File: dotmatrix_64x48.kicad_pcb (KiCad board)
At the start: 2 copper layers, 226 x 136 mm, 512 parts, among them J1 CONN_01X04, J2 CONN_01X05, P3 CONN_01X06, P6 CONN_01X03, Q1 Q_NPN_BCE RN5006, Q10 AO3401, Q11 AO3401, Q12 AO3401, Q13 AO3401, Q14 AO3401, Q15 AO3401, Q16 AO3401, Q17 AO3401, Q18 AO3401, Q19 AO3401, Q2 Q_NPN_BEC, Q20 AO3401, Q21 AO3401, Q22 AO3401, Q23 AO3401, Q24 AO3401, Q25 AO3401, Q26 AO3401, Q27 AO3401, Q28 AO3401, Q29 AO3401, Q3 NJL7302L-F3, Q30 Q_NPN_BEC, Q4 Q_NPN_BEC, Q5 AO3401, Q6 AO3401, Q7 AO3401, Q8 AO3401, Q9 AO3401, SW1 SW_PUSH_SMALL_H, SW2 SW_PUSH_SMALL_H, SW3 SW_PUSH_SMALL_H, SW4 SW_PUSH_SMALL_H, SW5 SW_PUSH_SMALL_H, SW6 SW_PUSH_SMALL_H, SW7 SW_PUSH_SMALL_H, SW8 SW_PUSH_SMALL_H, T1 COMMON_MODE_CHOKE, U1 WROOM-02, U10 LED1642GW, U11 74HCT595, U12 AE-BME280, U13 74HCT595, U14 NJM2845DL1-33, U15 74HCT595, U17 OSRB38C9AA, U18 BME280, U19 PIC32MX220F032B-I/ML, U2 74VHC541, U3 LED1642GW, U4 LED1642GW, U5 LED1642GW, U6 LED1642GW, U7 LED1642GW, U8 LED1642GW, U9 LED1642GW, Y1 8MHz

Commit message: Layout almost complete.
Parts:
- removed the REF** at (49.0, 13.1)
- removed the REF** at (46.0, 42.1)
- removed the REF** at (46.0, 41.0)
- added REF**: stitch-via-0.6mm, components:stitch-via-0.6mm, F.Cu at (41.3, 102.9)
- added REF**: stitch-via-0.6mm, components:stitch-via-0.6mm, F.Cu at (45.8, 133.9)
- added REF**: stitch-via-0.6mm, components:stitch-via-0.6mm, F.Cu at (226.2, 126.9)
- added REF**: stitch-via-0.6mm, components:stitch-via-0.6mm, F.Cu at (226.0, 137.4)
- added REF**: stitch-via-0.6mm, components:stitch-via-0.6mm, F.Cu at (222.8, 135.1)
- added REF**: stitch-via-0.6mm, components:stitch-via-0.6mm, F.Cu at (218.6, 135.1)
- added REF**: stitch-via-0.6mm, components:stitch-via-0.6mm, F.Cu at (214.5, 135.4)
- added REF**: stitch-via-0.6mm, components:stitch-via-0.6mm, F.Cu at (202.8, 135.6)
- added REF**: stitch-via-0.6mm, components:stitch-via-0.6mm, F.Cu at (194.1, 135.7)
- added REF**: stitch-via-0.6mm, components:stitch-via-0.6mm, F.Cu at (190.7, 135.5)
- added REF**: stitch-via-0.6mm, components:stitch-via-0.6mm, F.Cu at (178.8, 135.7)
- added REF**: stitch-via-0.6mm, components:stitch-via-0.6mm, F.Cu at (170.2, 135.4)
- added REF**: stitch-via-0.6mm, components:stitch-via-0.6mm, F.Cu at (44.5, 134.5)
- added REF**: stitch-via-0.6mm, components:stitch-via-0.6mm, F.Cu at (153.9, 135.7)
- added REF**: stitch-via-0.6mm, components:stitch-via-0.6mm, F.Cu at (150.3, 135.7)
- added REF**: stitch-via-0.6mm, components:stitch-via-0.6mm, F.Cu at (146.3, 135.7)
- added REF**: stitch-via-0.6mm, components:stitch-via-0.6mm, F.Cu at (137.8, 135.4)
- added REF**: stitch-via-0.6mm, components:stitch-via-0.6mm, F.Cu at (133.3, 135.7)
- added REF**: stitch-via-0.6mm, components:stitch-via-0.6mm, F.Cu at (129.8, 135.5)
- added REF**: stitch-via-0.6mm, components:stitch-via-0.6mm, F.Cu at (117.7, 135.5)
- added REF**: stitch-via-0.6mm, components:stitch-via-0.6mm, F.Cu at (109.8, 135.4)
- added REF**: stitch-via-0.6mm, components:stitch-via-0.6mm, F.Cu at (92.5, 135.7)
- added REF**: stitch-via-0.6mm, components:stitch-via-0.6mm, F.Cu at (84.5, 134.8)
- added REF**: stitch-via-0.6mm, components:stitch-via-0.6mm, F.Cu at (45.7, 135.4)
- added REF**: stitch-via-0.6mm, components:stitch-via-0.6mm, F.Cu at (80.9, 133.6)
- added REF**: stitch-via-0.6mm, components:stitch-via-0.6mm, F.Cu at (71.9, 134.4)
- added REF**: stitch-via-0.6mm, components:stitch-via-0.6mm, F.Cu at (75.8, 128.0)
- added REF**: stitch-via-0.6mm, components:stitch-via-0.6mm, F.Cu at (80.2, 128.0)
- added REF**: stitch-via-0.6mm, components:stitch-via-0.6mm, F.Cu at (85.0, 127.5)
- added REF**: stitch-via-0.6mm, components:stitch-via-0.6mm, F.Cu at (92.5, 127.0)
- added REF**: stitch-via-0.6mm, components:stitch-via-0.6mm, F.Cu at (98.0, 127.0)
- added REF**: stitch-via-0.6mm, components:stitch-via-0.6mm, F.Cu at (105.8, 126.9)
- added REF**: stitch-via-0.6mm, components:stitch-via-0.6mm, F.Cu at (112.0, 126.8)
- added REF**: stitch-via-0.6mm, components:stitch-via-0.6mm, F.Cu at (118.5, 126.9)
- added REF**: stitch-via-0.6mm, components:stitch-via-0.6mm, F.Cu at (43.6, 135.8)
- added REF**: stitch-via-0.6mm, components:stitch-via-0.6mm, F.Cu at (121.0, 127.0)
- added REF**: stitch-via-0.6mm, components:stitch-via-0.6mm, F.Cu at (125.6, 126.9)
- added REF**: stitch-via-0.6mm, components:stitch-via-0.6mm, F.Cu at (132.5, 127.0)
- added REF**: stitch-via-0.6mm, components:stitch-via-0.6mm, F.Cu at (138.8, 127.0)
- added REF**: stitch-via-0.6mm, components:stitch-via-0.6mm, F.Cu at (146.2, 126.8)
- added REF**: stitch-via-0.6mm, components:stitch-via-0.6mm, F.Cu at (153.1, 127.0)
- added REF**: stitch-via-0.6mm, components:stitch-via-0.6mm, F.Cu at (158.8, 127.0)
- added REF**: stitch-via-0.6mm, components:stitch-via-0.6mm, F.Cu at (173.4, 127.0)
- added REF**: stitch-via-0.6mm, components:stitch-via-0.6mm, F.Cu at (179.2, 127.0)
- added REF**: stitch-via-0.6mm, components:stitch-via-0.6mm, F.Cu at (181.8, 126.9)
- added REF**: stitch-via-0.6mm, components:stitch-via-0.6mm, F.Cu at (39.6, 136.1)
- added REF**: stitch-via-0.6mm, components:stitch-via-0.6mm, F.Cu at (186.8, 126.9)
- added REF**: stitch-via-0.6mm, components:stitch-via-0.6mm, F.Cu at (193.7, 127.1)
- added REF**: stitch-via-0.6mm, components:stitch-via-0.6mm, F.Cu at (199.7, 127.2)
- added REF**: stitch-via-0.6mm, components:stitch-via-0.6mm, F.Cu at (196.9, 127.1)
- added REF**: stitch-via-0.6mm, components:stitch-via-0.6mm, F.Cu at (211.3, 127.0)
- added REF**: stitch-via-0.6mm, components:stitch-via-0.6mm, F.Cu at (206.9, 127.0)
- added REF**: stitch-via-0.6mm, components:stitch-via-0.6mm, F.Cu at (213.6, 127.0)
- added REF**: stitch-via-0.6mm, components:stitch-via-0.6mm, F.Cu at (219.8, 127.0)
- added REF**: stitch-via-0.6mm, components:stitch-via-0.6mm, F.Cu at (208.4, 106.5)
- added REF**: stitch-via-0.6mm, components:stitch-via-0.6mm, F.Cu at (187.8, 106.8)
- added REF**: stitch-via-0.6mm, components:stitch-via-0.6mm, F.Cu at (67.1, 134.2)
- added REF**: stitch-via-0.6mm, components:stitch-via-0.6mm, F.Cu at (167.7, 106.6)
- added REF**: stitch-via-0.6mm, components:stitch-via-0.6mm, F.Cu at (127.0, 106.8)
- added REF**: stitch-via-0.6mm, components:stitch-via-0.6mm, F.Cu at (147.1, 106.7)
- added REF**: stitch-via-0.6mm, components:stitch-via-0.6mm, F.Cu at (106.9, 66.7)
- added REF**: stitch-via-0.6mm, components:stitch-via-0.6mm, F.Cu at (147.7, 66.5)
- added REF**: stitch-via-0.6mm, components:stitch-via-0.6mm, F.Cu at (127.2, 66.5)
- added REF**: stitch-via-0.6mm, components:stitch-via-0.6mm, F.Cu at (168.1, 66.5)
- added REF**: stitch-via-0.6mm, components:stitch-via-0.6mm, F.Cu at (207.5, 67.0)
- added REF**: stitch-via-0.6mm, components:stitch-via-0.6mm, F.Cu at (220.6, 66.8)
- added REF**: stitch-via-0.6mm, components:stitch-via-0.6mm, F.Cu at (76.8, 59.7)
- added REF**: stitch-via-0.6mm, components:stitch-via-0.6mm, F.Cu at (70.2, 58.8)
- added REF**: stitch-via-0.6mm, components:stitch-via-0.6mm, F.Cu at (75.1, 19.3)
- added REF**: stitch-via-0.6mm, components:stitch-via-0.6mm, F.Cu at (77.7, 19.2)
- added REF**: stitch-via-0.6mm, components:stitch-via-0.6mm, F.Cu at (88.8, 24.2)
- added REF**: stitch-via-0.6mm, components:stitch-via-0.6mm, F.Cu at (84.6, 24.2)
- added REF**: stitch-via-0.6mm, components:stitch-via-0.6mm, F.Cu at (98.0, 19.1)
- added REF**: stitch-via-0.6mm, components:stitch-via-0.6mm, F.Cu at (95.7, 18.8)
- added REF**: stitch-via-0.6mm, components:stitch-via-0.6mm, F.Cu at (95.5, 24.4)
- added REF**: stitch-via-0.6mm, components:stitch-via-0.6mm, F.Cu at (109.2, 23.8)
- added REF**: stitch-via-0.6mm, components:stitch-via-0.6mm, F.Cu at (104.5, 24.0)
- added REF**: stitch-via-0.6mm, components:stitch-via-0.6mm, F.Cu at (117.7, 19.1)
- added REF**: stitch-via-0.6mm, components:stitch-via-0.6mm, F.Cu at (69.2, 100.7)
- added REF**: stitch-via-0.6mm, components:stitch-via-0.6mm, F.Cu at (115.8, 19.1)
- added REF**: stitch-via-0.6mm, components:stitch-via-0.6mm, F.Cu at (129.4, 24.0)
- added REF**: stitch-via-0.6mm, components:stitch-via-0.6mm, F.Cu at (124.8, 24.2)
- added REF**: stitch-via-0.6mm, components:stitch-via-0.6mm, F.Cu at (149.3, 24.1)
- added REF**: stitch-via-0.6mm, components:stitch-via-0.6mm, F.Cu at (145.4, 24.1)
- added REF**: stitch-via-0.6mm, components:stitch-via-0.6mm, F.Cu at (156.4, 19.0)
- added REF**: stitch-via-0.6mm, components:stitch-via-0.6mm, F.Cu at (158.4, 18.9)
- added REF**: stitch-via-0.6mm, components:stitch-via-0.6mm, F.Cu at (170.0, 24.1)
- added REF**: stitch-via-0.6mm, components:stitch-via-0.6mm, F.Cu at (165.8, 24.1)
- added REF**: stitch-via-0.6mm, components:stitch-via-0.6mm, F.Cu at (190.2, 24.0)
- added REF**: stitch-via-0.6mm, components:stitch-via-0.6mm, F.Cu at (211.8, 85.7)
- added REF**: stitch-via-0.6mm, components:stitch-via-0.6mm, F.Cu at (186.0, 24.1)
- added REF**: stitch-via-0.6mm, components:stitch-via-0.6mm, F.Cu at (206.4, 24.5)
- added REF**: stitch-via-0.6mm, components:stitch-via-0.6mm, F.Cu at (210.2, 24.5)
- added REF**: stitch-via-0.6mm, components:stitch-via-0.6mm, F.Cu at (178.0, 18.9)
- added REF**: stitch-via-0.6mm, components:stitch-via-0.6mm, F.Cu at (176.8, 18.9)
- added REF**: stitch-via-0.6mm, components:stitch-via-0.6mm, F.Cu at (198.9, 19.4)
- added REF**: stitch-via-0.6mm, components:stitch-via-0.6mm, F.Cu at (196.9, 19.3)
- added REF**: stitch-via-0.6mm, components:stitch-via-0.6mm, F.Cu at (217.5, 24.5)
- added REF**: stitch-via-0.6mm, components:stitch-via-0.6mm, F.Cu at (208.2, 26.1)
- added REF**: stitch-via-0.6mm, components:stitch-via-0.6mm, F.Cu at (197.2, 24.4)
- added REF**: stitch-via-0.6mm, components:stitch-via-0.6mm, F.Cu at (208.7, 86.6)
- added REF**: stitch-via-0.6mm, components:stitch-via-0.6mm, F.Cu at (188.1, 26.1)
- added REF**: stitch-via-0.6mm, components:stitch-via-0.6mm, F.Cu at (176.8, 24.4)
- added REF**: stitch-via-0.6mm, components:stitch-via-0.6mm, F.Cu at (167.5, 26.1)
- added REF**: stitch-via-0.6mm, components:stitch-via-0.6mm, F.Cu at (156.5, 24.4)
- added REF**: stitch-via-0.6mm, components:stitch-via-0.6mm, F.Cu at (147.4, 26.0)
- added REF**: stitch-via-0.6mm, components:stitch-via-0.6mm, F.Cu at (136.6, 24.4)
- added REF**: stitch-via-0.6mm, components:stitch-via-0.6mm, F.Cu at (127.1, 25.8)
- added REF**: stitch-via-0.6mm, components:stitch-via-0.6mm, F.Cu at (116.0, 24.4)
- added REF**: stitch-via-0.6mm, components:stitch-via-0.6mm, F.Cu at (106.9, 26.0)
- added REF**: stitch-via-0.6mm, components:stitch-via-0.6mm, F.Cu at (86.9, 26.3)
- added REF**: stitch-via-0.6mm, components:stitch-via-0.6mm, F.Cu at (32.3, 101.5)
- added REF**: stitch-via-0.6mm, components:stitch-via-0.6mm, F.Cu at (188.4, 86.3)
- added REF**: stitch-via-0.6mm, components:stitch-via-0.6mm, F.Cu at (75.4, 24.3)
- added REF**: stitch-via-0.6mm, components:stitch-via-0.6mm, F.Cu at (69.3, 23.9)
- added REF**: stitch-via-0.6mm, components:stitch-via-0.6mm, F.Cu at (70.0, 22.1)
- added REF**: stitch-via-0.6mm, components:stitch-via-0.6mm, F.Cu at (69.8, 20.3)
- added REF**: stitch-via-0.6mm, components:stitch-via-0.6mm, F.Cu at (70.6, 18.9)
- added REF**: stitch-via-0.6mm, components:stitch-via-0.6mm, F.Cu at (30.6, 88.2)
- added REF**: stitch-via-0.6mm, components:stitch-via-0.6mm, F.Cu at (46.1, 94.7)
- added REF**: stitch-via-0.6mm, components:stitch-via-0.6mm, F.Cu at (43.5, 96.6)
- added REF**: stitch-via-0.6mm, components:stitch-via-0.6mm, F.Cu at (34.0, 88.8)
- added REF**: stitch-via-0.6mm, components:stitch-via-0.6mm, F.Cu at (168.2, 86.4)
- added REF**: stitch-via-0.6mm, components:stitch-via-0.6mm, F.Cu at (29.2, 91.2)
- added REF**: stitch-via-0.6mm, components:stitch-via-0.6mm, F.Cu at (47.4, 87.0)
- added REF**: stitch-via-0.6mm, components:stitch-via-0.6mm, F.Cu at (24.4, 108.5)
- added REF**: stitch-via-0.6mm, components:stitch-via-0.6mm, F.Cu at (22.8, 108.2)
- added REF**: stitch-via-0.6mm, components:stitch-via-0.6mm, F.Cu at (147.7, 86.3)
- added REF**: stitch-via-0.6mm, components:stitch-via-0.6mm, F.Cu at (212.7, 147.0)
- added REF**: stitch-via-0.6mm, components:stitch-via-0.6mm, F.Cu at (196.3, 147.0)
- added REF**: stitch-via-0.6mm, components:stitch-via-0.6mm, F.Cu at (174.4, 146.9)
- added REF**: stitch-via-0.6mm, components:stitch-via-0.6mm, F.Cu at (154.3, 146.8)
- added REF**: stitch-via-0.6mm, components:stitch-via-0.6mm, F.Cu at (133.7, 146.9)
- added REF**: stitch-via-0.6mm, components:stitch-via-0.6mm, F.Cu at (113.5, 147.0)
- added REF**: stitch-via-0.6mm, components:stitch-via-0.6mm, F.Cu at (86.7, 146.8)
- added REF**: stitch-via-0.6mm, components:stitch-via-0.6mm, F.Cu at (36.6, 103.8)
- added REF**: stitch-via-0.6mm, components:stitch-via-0.6mm, F.Cu at (71.5, 16.7)
- added REF**: stitch-via-0.6mm, components:stitch-via-0.6mm, F.Cu at (138.0, 19.1)
- added REF**: stitch-via-0.6mm, components:stitch-via-0.6mm, F.Cu at (136.3, 19.2)
- added REF**: stitch-via-0.6mm, components:stitch-via-0.6mm, F.Cu at (234.4, 24.4)
- added REF**: stitch-via-0.6mm, components:stitch-via-0.6mm, F.Cu at (234.2, 22.7)
- added REF**: stitch-via-0.6mm, components:stitch-via-0.6mm, F.Cu at (228.6, 30.3)
- added REF**: stitch-via-0.6mm, components:stitch-via-0.6mm, F.Cu at (204.0, 17.7)
- added REF**: stitch-via-0.6mm, components:stitch-via-0.6mm, F.Cu at (219.4, 19.5)
- added REF**: stitch-via-0.6mm, components:stitch-via-0.6mm, F.Cu at (217.8, 19.2)
- added REF**: stitch-via-0.6mm, components:stitch-via-0.6mm, F.Cu at (57.2, 86.3)
- added REF**: stitch-via-0.6mm, components:stitch-via-0.6mm, F.Cu at (38.4, 109.7)
- added REF**: stitch-via-0.6mm, components:stitch-via-0.6mm, F.Cu at (38.1, 53.9)
- added REF**: stitch-via-0.6mm, components:stitch-via-0.6mm, F.Cu at (22.7, 34.8)
- added REF**: stitch-via-0.6mm, components:stitch-via-0.6mm, F.Cu at (22.9, 33.7)
- added REF**: stitch-via-0.6mm, components:stitch-via-0.6mm, F.Cu at (22.8, 32.6)
- added REF**: stitch-via-0.6mm, components:stitch-via-0.6mm, F.Cu at (22.8, 31.5)
- added REF**: stitch-via-0.6mm, components:stitch-via-0.6mm, F.Cu at (26.6, 31.8)
- added REF**: stitch-via-0.6mm, components:stitch-via-0.6mm, F.Cu at (24.1, 31.8)
- added REF**: stitch-via-0.6mm, components:stitch-via-0.6mm, F.Cu at (24.3, 34.6)
- added REF**: stitch-via-0.6mm, components:stitch-via-0.6mm, F.Cu at (26.8, 34.6)
- added REF**: stitch-via-0.6mm, components:stitch-via-0.6mm, F.Cu at (27.9, 34.4)
- added REF**: stitch-via-0.6mm, components:stitch-via-0.6mm, F.Cu at (35.3, 136.6)
- added REF**: stitch-via-0.6mm, components:stitch-via-0.6mm, F.Cu at (27.9, 33.4)
- added REF**: stitch-via-0.6mm, components:stitch-via-0.6mm, F.Cu at (27.8, 32.4)
- added REF**: stitch-via-0.6mm, components:stitch-via-0.6mm, F.Cu at (27.9, 31.5)
- added REF**: stitch-via-0.6mm, components:stitch-via-0.6mm, F.Cu at (22.6, 14.7)
- added REF**: stitch-via-0.6mm, components:stitch-via-0.6mm, F.Cu at (43.6, 87.0)
- added REF**: stitch-via-0.6mm, components:stitch-via-0.6mm, F.Cu at (47.8, 123.7)
- added REF**: stitch-via-0.6mm, components:stitch-via-0.6mm, F.Cu at (48.5, 122.5)
- added REF**: stitch-via-0.6mm, components:stitch-via-0.6mm, F.Cu at (34.8, 123.4)
- added REF**: stitch-via-0.6mm, components:stitch-via-0.6mm, F.Cu at (32.2, 126.0)
- added REF**: stitch-via-0.6mm, components:stitch-via-0.6mm, F.Cu at (39.3, 124.0)
- added REF**: stitch-via-0.6mm, components:stitch-via-0.6mm, F.Cu at (44.4, 131.7)
- added REF**: stitch-via-0.6mm, components:stitch-via-0.6mm, F.Cu at (40.9, 123.8)
- added REF**: stitch-via-0.6mm, components:stitch-via-0.6mm, F.Cu at (42.3, 123.5)
- added REF**: stitch-via-0.6mm, components:stitch-via-0.6mm, F.Cu at (39.6, 122.7)
- added REF**: stitch-via-0.6mm, components:stitch-via-0.6mm, F.Cu at (38.4, 122.7)
- added REF**: stitch-via-0.6mm, components:stitch-via-0.6mm, F.Cu at (41.2, 122.7)
- added REF**: stitch-via-0.6mm, components:stitch-via-0.6mm, F.Cu at (40.5, 129.4)
- added REF**: stitch-via-0.6mm, components:stitch-via-0.6mm, F.Cu at (32.2, 140.3)
- added REF**: stitch-via-0.6mm, components:stitch-via-0.6mm, F.Cu at (24.6, 112.5)
- added REF**: stitch-via-0.6mm, components:stitch-via-0.6mm, F.Cu at (33.6, 110.6)
- added REF**: stitch-via-0.6mm, components:stitch-via-0.6mm, F.Cu at (66.0, 42.5)
- added REF**: stitch-via-0.6mm, components:stitch-via-0.6mm, F.Cu at (46.2, 126.2)
- added REF**: stitch-via-0.6mm, components:stitch-via-0.6mm, F.Cu at (47.9, 38.9)
- added REF**: stitch-via-0.6mm, components:stitch-via-0.6mm, F.Cu at (45.5, 32.7)
- added REF**: stitch-via-0.6mm, components:stitch-via-0.6mm, F.Cu at (46.2, 40.6)
- added REF**: stitch-via-0.6mm, components:stitch-via-0.6mm, F.Cu at (222.9, 16.4)
- added REF**: stitch-via-0.6mm, components:stitch-via-0.6mm, F.Cu at (209.3, 16.7)
- added REF**: stitch-via-0.6mm, components:stitch-via-0.6mm, F.Cu at (188.4, 16.6)
- added REF**: stitch-via-0.6mm, components:stitch-via-0.6mm, F.Cu at (168.3, 16.8)
- added REF**: stitch-via-0.6mm, components:stitch-via-0.6mm, F.Cu at (148.8, 16.6)
- added REF**: stitch-via-0.6mm, components:stitch-via-0.6mm, F.Cu at (127.6, 16.8)
- added REF**: stitch-via-0.6mm, components:stitch-via-0.6mm, F.Cu at (107.4, 17.0)
- added REF**: stitch-via-0.6mm, components:stitch-via-0.6mm, F.Cu at (47.1, 137.7)
- added REF**: stitch-via-0.6mm, components:stitch-via-0.6mm, F.Cu at (86.7, 16.9)
- added REF**: stitch-via-0.6mm, components:stitch-via-0.6mm, F.Cu at (61.1, 24.1)
- added REF**: stitch-via-0.6mm, components:stitch-via-0.6mm, F.Cu at (66.4, 18.6)
- added REF**: stitch-via-0.6mm, components:stitch-via-0.6mm, F.Cu at (225.9, 13.3)
- added REF**: stitch-via-0.6mm, components:stitch-via-0.6mm, F.Cu at (150.8, 13.0)
- added REF**: stitch-via-0.6mm, components:stitch-via-0.6mm, F.Cu at (69.0, 13.0)
- added REF**: stitch-via-0.6mm, components:stitch-via-0.6mm, F.Cu at (228.4, 106.5)
- added REF**: stitch-via-0.6mm, components:stitch-via-0.6mm, F.Cu at (228.4, 86.1)
- added REF**: stitch-via-0.6mm, components:stitch-via-0.6mm, F.Cu at (228.0, 66.6)
- added REF**: stitch-via-0.6mm, components:stitch-via-0.6mm, F.Cu at (226.2, 23.8)
- added REF**: stitch-via-0.6mm, components:stitch-via-0.6mm, F.Cu at (43.3, 137.6)
- added REF**: stitch-via-0.6mm, components:stitch-via-0.6mm, F.Cu at (236.0, 32.5)
- added REF**: stitch-via-0.6mm, components:stitch-via-0.6mm, F.Cu at (236.3, 43.8)
- added REF** (x2): stitch-via-0.6mm, components:stitch-via-0.6mm, F.Cu at (236.0, 55.5)
- added REF**: stitch-via-0.6mm, components:stitch-via-0.6mm, F.Cu at (236.3, 65.9)
- added REF**: stitch-via-0.6mm, components:stitch-via-0.6mm, F.Cu at (236.3, 77.8)
- added REF**: stitch-via-0.6mm, components:stitch-via-0.6mm, F.Cu at (236.6, 89.7)
- added REF**: stitch-via-0.6mm, components:stitch-via-0.6mm, F.Cu at (236.0, 104.7)
- added REF**: stitch-via-0.6mm, components:stitch-via-0.6mm, F.Cu at (236.2, 116.9)
- added REF**: stitch-via-0.6mm, components:stitch-via-0.6mm, F.Cu at (236.1, 130.8)
- moved REF** 24.7 mm to (39.2, 82.7)
- moved W19 23.0 mm to (225.3, 16.7)
- moved R131 20.4 mm to (228.2, 16.7), turned to 0 degrees
- moved R133 17.6 mm to (231.3, 22.9), turned to 0 degrees
- moved R132 14.8 mm to (228.2, 18.3), turned to 0 degrees
- moved C13 12.1 mm to (50.9, 45.5)
- moved W4 7.76 mm to (40.1, 15.1)
- moved REF** 7.58 mm to (39.6, 94.2)
- moved REF** 5.82 mm to (43.9, 92.8)
- moved R134 3.01 mm to (231.3, 24.4)
- moved REF** 2.58 mm to (19.5, 79.7)
- moved C23 2.50 mm to (45.7, 41.5), turned to 90 degrees
- moved C87 2.36 mm to (227.7, 21.2)
- moved W16 2.18 mm to (195.2, 17.7)
- moved W18 1.86 mm to (215.5, 17.8)
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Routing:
- net GND: track 725.0 -> 5271.3 mm, vias 52 -> 392
- net LED1642VDD: track 71.0 -> 276.2 mm, vias 3 -> 10
- net COLSEROUT: track 44.6 -> 234.5 mm, vias 3 -> 7
- net COLPWCLK0: track 62.9 -> 235.9 mm, vias 2 -> 9
- net COLPWCLK1: track 74.6 -> 242.2 mm, vias 2 -> 9
- net COLLATCH: track 71.4 -> 227.5 mm, vias 17 -> 10
- net COLCLK: track 92.2 -> 225.1 mm, vias 4 -> 10
- net LEDVDD: track 254.1 -> 328.6 mm
- net r9: track 356.2 -> 377.9 mm, vias 4 -> 5
- net Net-(U4-Pad22): track 0.00 -> 18.6 mm, vias 0 -> 2
- net Net-(U3-Pad22): track 0.00 -> 18.3 mm, vias 0 -> 2
- net Net-(U6-Pad22): track 0.00 -> 17.8 mm, vias 0 -> 2
- net Net-(U10-Pad2): track 0.00 -> 17.8 mm, vias 0 -> 2
- net r1: track 361.4 -> 379.1 mm
- net Net-(U5-Pad22): track 0.00 -> 17.6 mm, vias 0 -> 2
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
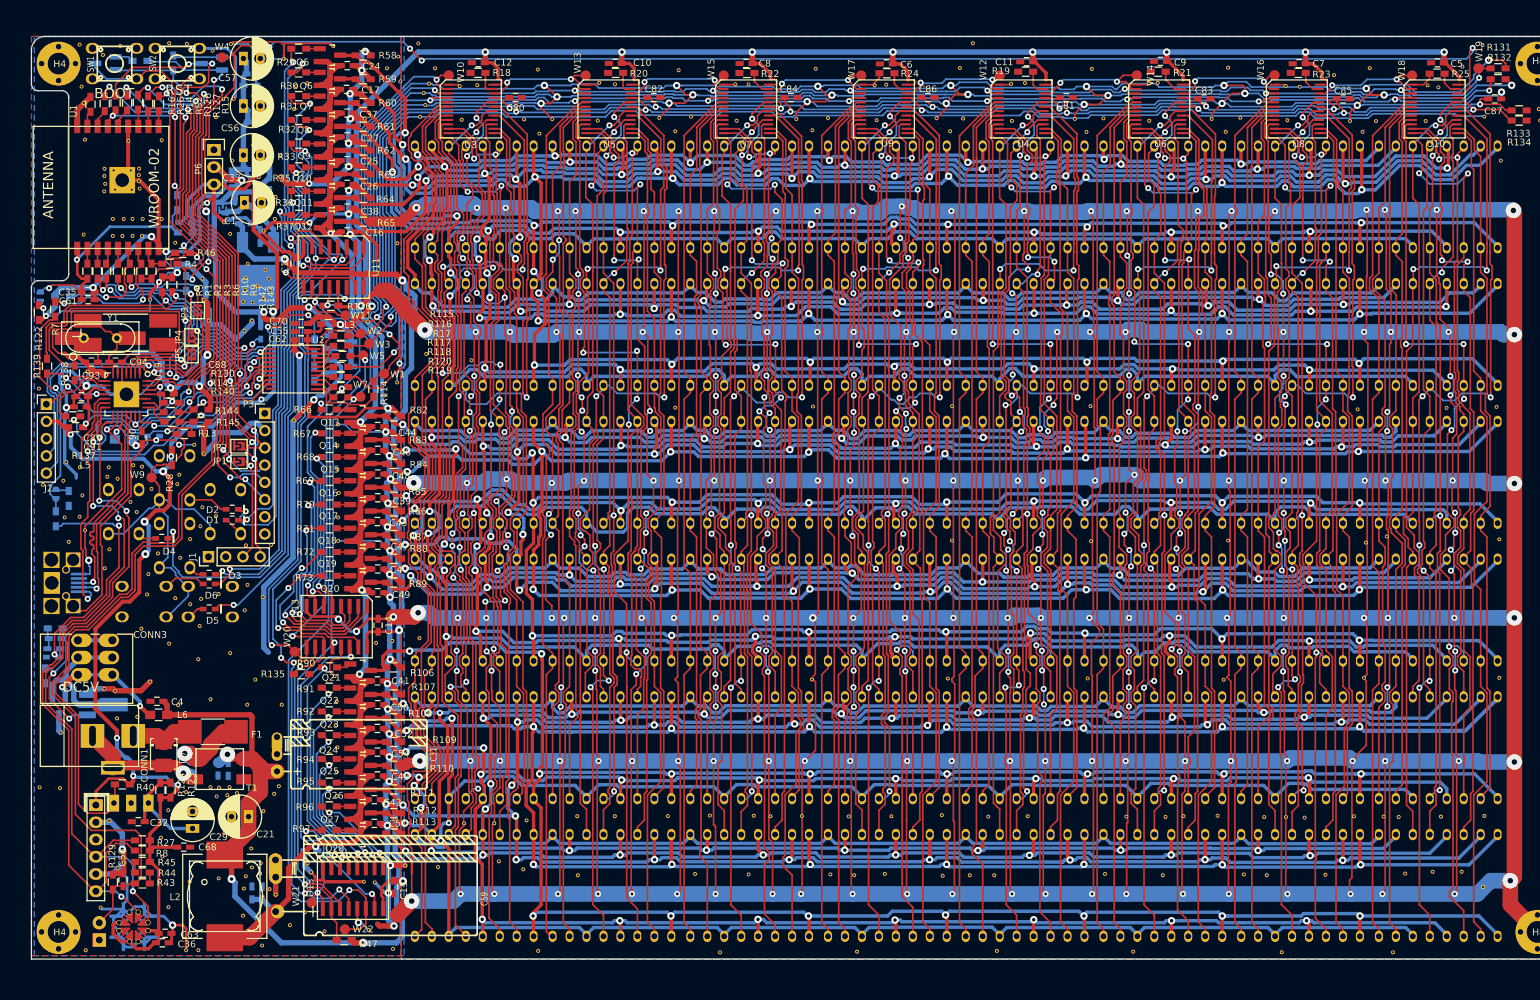
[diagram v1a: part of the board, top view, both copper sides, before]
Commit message: Silk fix; Pattern pull out from ICs fiexed; Vias on pads fixed
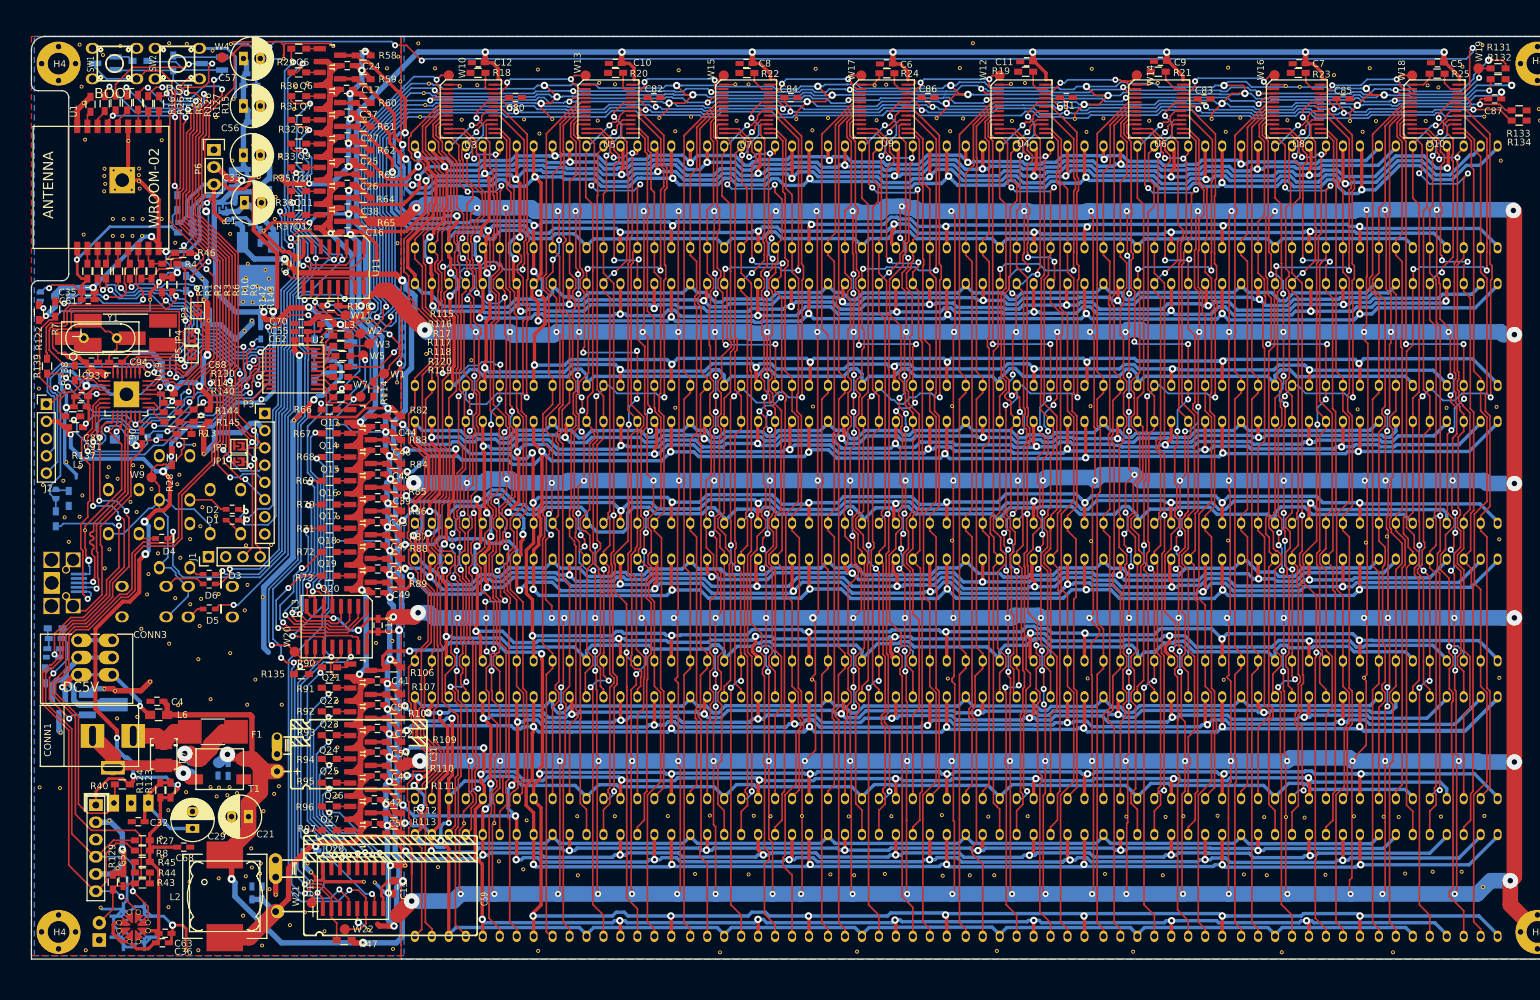
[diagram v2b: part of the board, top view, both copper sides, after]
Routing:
- net COLCLK: track 225.1 -> 228.7 mm
- net GND: track 5271.3 -> 5268.2 mm
- net COLLATCH: track 227.5 -> 229.7 mm
- net HC595LATCH: track 112.3 -> 114.0 mm
- net r0: track 411.8 -> 410.7 mm
- net COLPWCLK1: track 242.2 -> 243.3 mm
- net ce42: track 90.5 -> 89.6 mm
- net co32: track 140.7 -> 141.5 mm
- net r7: track 417.4 -> 416.7 mm
- net COLPWCLK0: track 235.9 -> 236.6 mm
- net ce21: track 113.2 -> 113.8 mm
- net ce37: track 112.9 -> 113.5 mm
- net co2: track 109.4 -> 110.0 mm
- net co21: track 139.3 -> 139.8 mm
- net ce22: track 106.9 -> 107.4 mm
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
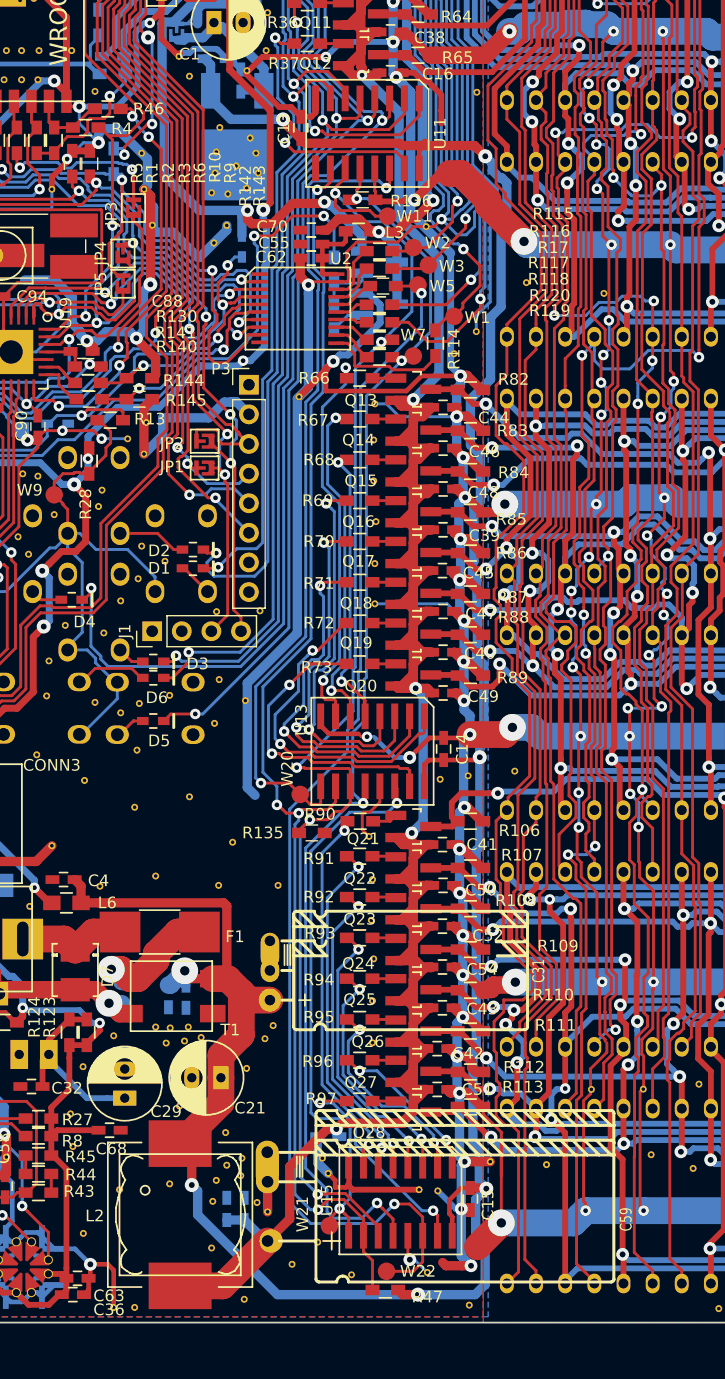
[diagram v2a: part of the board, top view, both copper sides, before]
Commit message: Set away thermelly active components from sensors; Silks and DRC not yet done
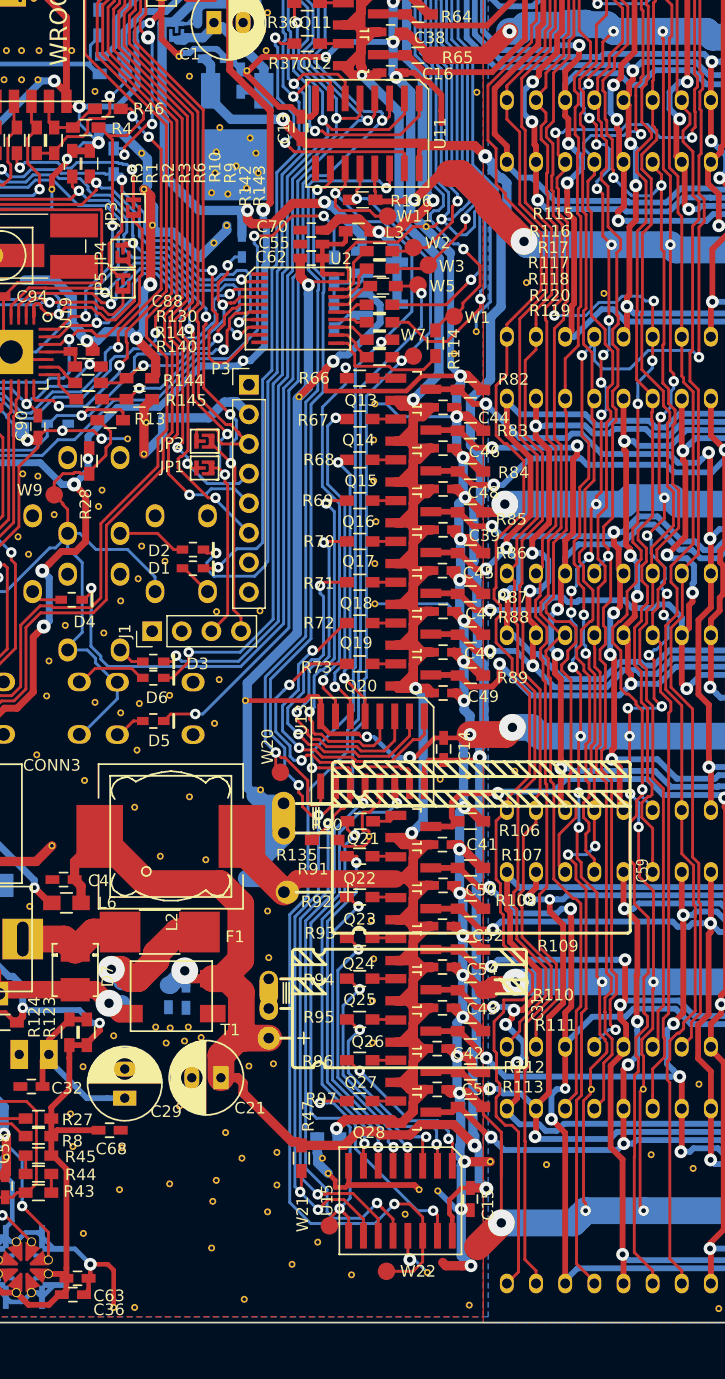
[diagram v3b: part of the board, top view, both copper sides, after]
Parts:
- removed the REF** at (48.9, 110.5)
- removed the REF** at (45.0, 106.8)
- removed the REF** at (57.0, 110.0)
- removed the REF** at (43.8, 110.5)
- removed the REF** at (38.4, 109.7)
- removed the REF** at (47.8, 123.7)
- removed the REF** at (48.5, 122.5)
- added REF**: stitch-via-0.6mm, components:stitch-via-0.6mm, F.Cu at (59.8, 138.7)
- added REF**: stitch-via-0.6mm, components:stitch-via-0.6mm, F.Cu at (35.5, 133.0)
- added REF**: stitch-via-0.6mm, components:stitch-via-0.6mm, F.Cu at (47.4, 102.3)
- added REF**: stitch-via-0.6mm, components:stitch-via-0.6mm, F.Cu at (48.1, 116.7)
- added REF**: stitch-via-0.6mm, components:stitch-via-0.6mm, F.Cu at (48.0, 112.7)
- added REF**: stitch-via-0.6mm, components:stitch-via-0.6mm, F.Cu at (38.8, 108.0)
- moved L2 32.5 mm to (39.7, 106.3), turned to 0 degrees
- moved C59 30.0 mm to (49.4, 111.1)
- moved C67 29.4 mm to (47.8, 108.9)
- moved C65 29.3 mm to (46.2, 109.0)
- moved R47 13.4 mm to (50.9, 133.9), turned to 270 degrees
- moved REF** 9.58 mm to (48.5, 125.8)
- moved REF** 9.36 mm to (42.7, 108.3)
- moved REF** 4.62 mm to (48.8, 133.4)
- moved C31 3.26 mm to (48.1, 123.6)
- moved REF** 3.20 mm to (48.8, 136.2)
- moved W20 2.55 mm to (49.1, 100.8)
- moved R135 1.25 mm to (52.9, 106.6)
- moved REF** 0.28 mm to (46.4, 126.0)
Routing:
- net GND: track 5268.2 -> 5288.8 mm
- net VCC: track 233.9 -> 215.2 mm, vias 7 -> 6
- net LEDVDD: track 328.7 -> 323.2 mm
- net Net-(R47-Pad2): track 112.2 -> 107.7 mm, vias 4 -> 5
- net HC595CLK: track 119.9 -> 118.0 mm
- net /row_driver/f_r8/IN6: track 29.8 -> 28.6 mm
- net /row_driver/f_r8/IN7: track 26.2 -> 25.3 mm
- net /row_driver/f_r8/IN5: track 30.8 -> 30.0 mm
- net /row_driver/f_r8/IN1: track 29.2 -> 28.5 mm
- net /row_driver/f_r8/IN4: track 31.7 -> 31.0 mm
- net /row_driver/f_r16/IN4: track 20.8 -> 21.4 mm
- net /row_driver/f_r16/IN6: track 13.8 -> 14.3 mm
- net HC595LATCH: track 114.0 -> 113.4 mm
- net /row_driver/f_r8/IN0: track 33.8 -> 33.3 mm
